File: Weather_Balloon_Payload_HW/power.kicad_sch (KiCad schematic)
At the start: 76 parts, among them J1 Conn_01x02, Q1 Si2302, Q2 Si2301, U1 AP3211K, U2 AP3211K, U3 ADP1612, U4 NCP308SN180T1G

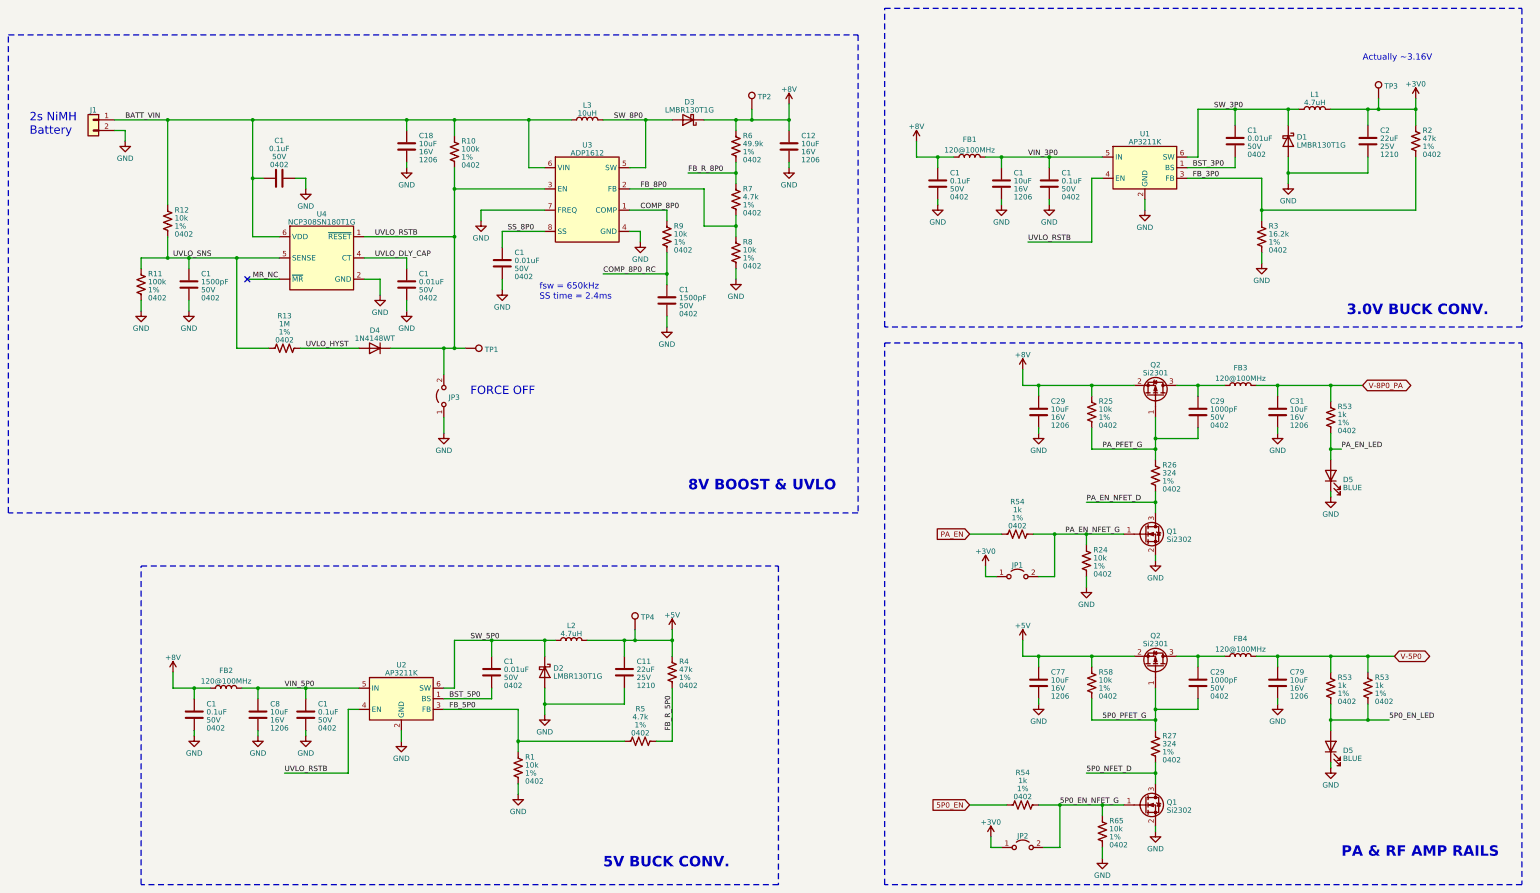
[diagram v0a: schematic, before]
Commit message: Update README, block diagrams, schem. Begin layout
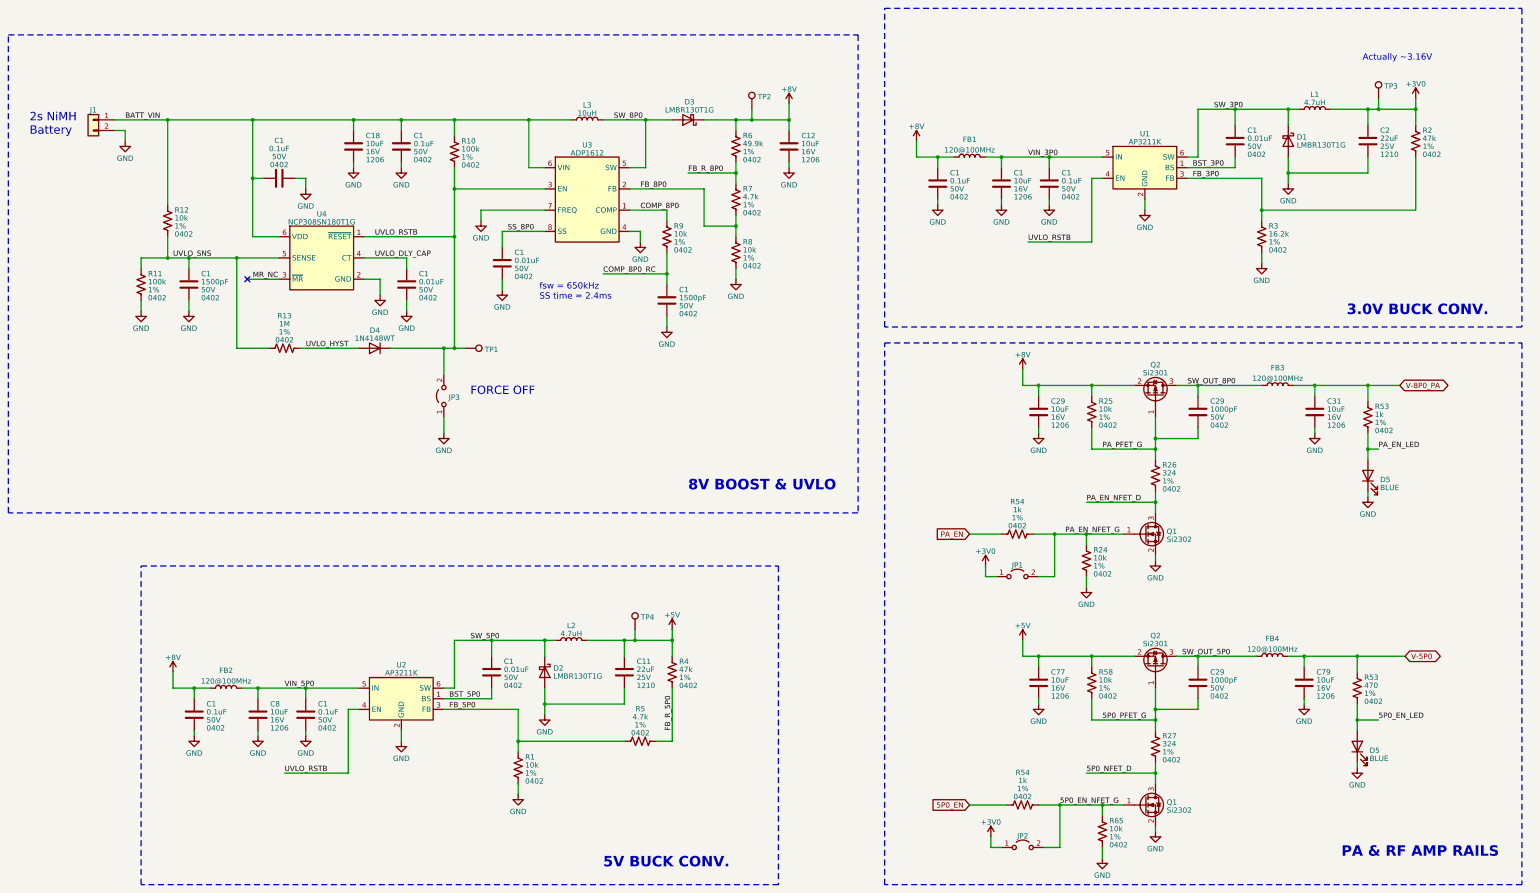
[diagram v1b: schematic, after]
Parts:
- removed R53: 1k, Resistor_SMD:R_0402_1005Metric, symbol Device:R_US
- added C1: 0.1uF, Capacitor_SMD:C_0402_1005Metric, symbol Device:C
- R53: value 1k -> 470; JLCPCB Part # C153104 -> (none); Manufacturer TA-I Tech -> (none); Mfr. Part # RM04JTN102 -> (none)
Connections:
- net BATT_VIN: now also C1.2
- net GND: now also C1.1
- net MR_NC: now also U4.3 (~{MR}); no longer U4. (~{MR})
- net SW_OUT_8P0: now reaches C29.2, FB3.1, Q2.3 (D)
- net SW_OUT_5P0: now reaches C29.2, FB4.1, Q2.3 (D)
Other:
- moved on the sheet: C18, C31, C79, D5, FB3, FB4, R53

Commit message: Add fabrication files
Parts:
- C1: JLCPCB Part # (none) -> C107022; Manufacturer (none) -> YAGEO; Mfr. Part # (none) -> CC0402KRX7R9BB152
- R2, R4: JLCPCB Part # (none) -> C284586; Manufacturer (none) -> Viking Tech; Mfr. Part # (none) -> ARG02FTC4702
- R26, R27: JLCPCB Part # (none) -> C423191; Manufacturer (none) -> UNI-ROYAL(Uniroyal Elec); Mfr. Part # (none) -> 0402WGF3240TCE
- R53: JLCPCB Part # (none) -> C103054; Manufacturer (none) -> RALEC; Mfr. Part # (none) -> RTT024700FTH
- U1, U2: JLCPCB Part # (none) -> C154863; Manufacturer (none) -> Diodes Incorporated; Mfr. Part # (none) -> AP3211KTR-G1
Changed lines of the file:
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@@
       (effects (font (size 1.27 1.27)) (justify left))
     )
-    (property "Mfr. Part #" "~" (at 182.88 88.9 0)
+    (property "Mfr. Part #" "CC0402KRX7R9BB152" (at 182.88 88.9 0)
       (effects (font (size 1.27 1.27)) hide)
     )
-    (property "JLCPCB Part #" "~" (at 182.88 88.9 0)
+    (property "JLCPCB Part #" "C107022" (at 182.88 88.9 0)
       (effects (font (size 1.27 1.27)) hide)
     )
@@
       (effects (font (size 1.27 1.27)) hide)
     )
-    (property "Manufacturer" "~" (at 182.88 88.9 0)
+    (property "Manufacturer" "YAGEO" (at 182.88 88.9 0)
       (effects (font (size 1.27 1.27)) hide)
     )
@@
       (effects (font (size 1.27 1.27)) (justify left))
     )
-    (property "Mfr. Part #" "~" (at 68.58 85.09 0)
+    (property "Mfr. Part #" "CC0402KRX7R9BB152" (at 68.58 85.09 0)
       (effects (font (size 1.27 1.27)) hide)
     )
-    (property "JLCPCB Part #" "~" (at 68.58 85.09 0)
+    (property "JLCPCB Part #" "C107022" (at 68.58 85.09 0)
       (effects (font (size 1.27 1.27)) hide)
     )
@@
       (effects (font (size 1.27 1.27)) hide)
     )
-    (property "Manufacturer" "~" (at 68.58 85.09 0)
+    (property "Manufacturer" "YAGEO" (at 68.58 85.09 0)
       (effects (font (size 1.27 1.27)) hide)
     )
@@
       (effects (font (size 1.27 1.27)) hide)
     )
-    (property "Description" "~" (at 184.15 177.8 0)
+    (property "Description" "62.5mW Thin Film Resistor ±25ppm/℃ ±1% 47kΩ 0402 Chip" (at 184.15 177.8 0)
       (effects (font (size 1.27 1.27)) hide)
     )
-    (property "JLCPCB Part #" "~" (at 184.15 177.8 0)
+    (property "JLCPCB Part #" "C284586" (at 184.15 177.8 0)
       (effects (font (size 1.27 1.27)) hide)
     )
-    (property "Manufacturer" "~" (at 184.15 177.8 0)
+    (property "Manufacturer" "Viking Tech" (at 184.15 177.8 0)
       (effects (font (size 1.27 1.27)) hide)
     )
-    (property "Mfr. Part #" "~" (at 184.15 177.8 0)
+    (property "Mfr. Part #" "ARG02FTC4702" (at 184.15 177.8 0)
       (effects (font (size 1.27 1.27)) hide)
     )
@@
       (effects (font (size 1.27 1.27)) hide)
     )
-    (property "Description" "~" (at 299.72 130.81 0)
+    (property "Description" "62.5mW Thick Film Resistors ±100ppm/℃ ±1% 324Ω 0402 Chip" (at 299.72 130.81 0)
       (effects (font (size 1.27 1.27)) hide)
     )
-    (property "JLCPCB Part #" "~" (at 299.72 130.81 0)
+    (property "JLCPCB Part #" "C423191" (at 299.72 130.81 0)
       (effects (font (size 1.27 1.27)) hide)
     )
-    (property "Manufacturer" "~" (at 299.72 130.81 0)
+    (property "Manufacturer" "UNI-ROYAL(Uniroyal Elec)" (at 299.72 130.81 0)
       (effects (font (size 1.27 1.27)) hide)
     )
-    (property "Mfr. Part #" "~" (at 299.72 130.81 0)
+    (property "Mfr. Part #" "0402WGF3240TCE" (at 299.72 130.81 0)
       (effects (font (size 1.27 1.27)) hide)
     )
@@
       (effects (font (size 1.27 1.27)) hide)
     )
-    (property "Description" "~" (at 361.95 50.8 0)
+    (property "Description" "62.5mW Thin Film Resistor ±25ppm/℃ ±1% 47kΩ 0402 Chip" (at 361.95 50.8 0)
       (effects (font (size 1.27 1.27)) hide)
     )
-    (property "JLCPCB Part #" "~" (at 361.95 50.8 0)
+    (property "JLCPCB Part #" "C284586" (at 361.95 50.8 0)
       (effects (font (size 1.27 1.27)) hide)
     )
-    (property "Manufacturer" "~" (at 361.95 50.8 0)
+    (property "Manufacturer" "Viking Tech" (at 361.95 50.8 0)
       (effects (font (size 1.27 1.27)) hide)
     )
-    (property "Mfr. Part #" "~" (at 361.95 50.8 0)
+    (property "Mfr. Part #" "ARG02FTC4702" (at 361.95 50.8 0)
       (effects (font (size 1.27 1.27)) hide)
     )
@@
       (effects (font (size 1.27 1.27)) hide)
     )
-    (property "Description" "~" (at 299.72 195.58 0)
+    (property "Description" "62.5mW Thick Film Resistors ±100ppm/℃ ±1% 324Ω 0402 Chip" (at 299.72 195.58 0)
       (effects (font (size 1.27 1.27)) hide)
     )
-    (property "JLCPCB Part #" "~" (at 299.72 195.58 0)
+    (property "JLCPCB Part #" "C423191" (at 299.72 195.58 0)
       (effects (font (size 1.27 1.27)) hide)
     )
-    (property "Manufacturer" "~" (at 299.72 195.58 0)
+    (property "Manufacturer" "UNI-ROYAL(Uniroyal Elec)" (at 299.72 195.58 0)
       (effects (font (size 1.27 1.27)) hide)
     )
-    (property "Mfr. Part #" "~" (at 299.72 195.58 0)
+    (property "Mfr. Part #" "0402WGF3240TCE" (at 299.72 195.58 0)
       (effects (font (size 1.27 1.27)) hide)
     )
@@
       (effects (font (size 1.27 1.27)) hide)
     )
+    (property "Description" "Step-down type Adjustable 0.81V~15V 1.5A 4.5V~18V SOT-23-6 DC-DC Converters" (at 119.38 184.15 0)
+      (effects (font (size 1.27 1.27)) hide)
+    )
+    (property "JLCPCB Part #" "C154863" (at 119.38 184.15 0)
+      (effects (font (size 1.27 1.27)) hide)
+    )
+    (property "Manufacturer" "Diodes Incorporated" (at 119.38 184.15 0)
+      (effects (font (size 1.27 1.27)) hide)
+    )
+    (property "Mfr. Part #" "AP3211KTR-G1" (at 119.38 184.15 0)
+      (effects (font (size 1.27 1.27)) hide)
+    )
     (pin "1")
     (pin "2")
@@
       (effects (font (size 1.27 1.27)) hide)
     )
+    (property "Description" "Step-down type Adjustable 0.81V~15V 1.5A 4.5V~18V SOT-23-6 DC-DC Converters" (at 297.18 57.15 0)
+      (effects (font (size 1.27 1.27)) hide)
+    )
+    (property "JLCPCB Part #" "C154863" (at 297.18 57.15 0)
+      (effects (font (size 1.27 1.27)) hide)
+    )
+    (property "Manufacturer" "Diodes Incorporated" (at 297.18 57.15 0)
+      (effects (font (size 1.27 1.27)) hide)
+    )
+    (property "Mfr. Part #" "AP3211KTR-G1" (at 297.18 57.15 0)
+      (effects (font (size 1.27 1.27)) hide)
+    )
     (pin "1")
     (pin "2")
@@
       (effects (font (size 1.27 1.27)) hide)
     )
-    (property "JLCPCB Part #" "~" (at 347.98 181.61 0)
+    (property "JLCPCB Part #" "C103054" (at 347.98 181.61 0)
       (effects (font (size 1.27 1.27)) hide)
     )
-    (property "Manufacturer" "~" (at 347.98 181.61 0)
+    (property "Manufacturer" "RALEC" (at 347.98 181.61 0)
       (effects (font (size 1.27 1.27)) hide)
     )
-    (property "Mfr. Part #" "~" (at 347.98 181.61 0)
+    (property "Mfr. Part #" "RTT024700FTH" (at 347.98 181.61 0)
       (effects (font (size 1.27 1.27)) hide)
     )
@@
       (effects (font (size 1.27 1.27)) (justify left))
     )
+    (property "Description" "62.5mW ±100ppm/℃ ±1% 470Ω 0402" (at 347.98 181.61 0)
+      (effects (font (size 1.27 1.27)) hide)
+    )
     (pin "1")
